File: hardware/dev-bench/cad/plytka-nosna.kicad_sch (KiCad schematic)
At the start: 69 parts, among them J1 ARDUINO POWER, J10 CC1120EM P2, J11 ANALIZATOR, J12 VTEST 0-15V, J2 ARDUINO A0-A5, J3 ARDUINO D0-D7, J4 ARDUINO D8-SCL, J5 DEVKITC J1, J6 DEVKITC J3, J7 SHARP LS027B7DH01A, J9 CC1120EM P1, Q1 MMBT3904, SW1 GÓRA, SW2 DÓŁ, SW3 OK, SW4 WSTECZ, SW5 CISZA, SW6 PRZYGOTOWANIE, U1 CY15B104QN-50SXI, U2 MCP1640

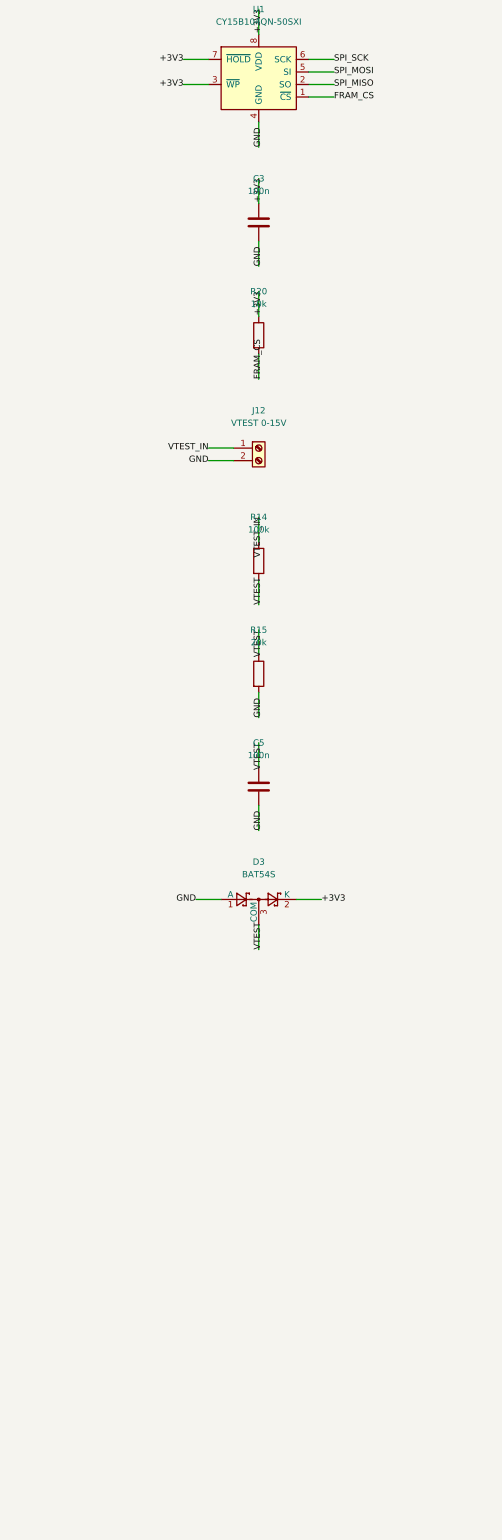
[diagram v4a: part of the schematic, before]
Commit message: Dev bench N1: hardware FRAM CS release on supply loss (audit vs F106)
The spec (elektronika.md, power loss, point 2) requires the FRAM CS to be
released before the FRAM supply drops below its minimum. The Arduino
RESET pin of the nRF52840-DK is not connected to the MCU (R45 not
fitted), so a supervisor on the MCU reset cannot do it on bench A.

- U3 TPS3840PH27 (push-pull active-high, 2.66-2.74 V) and U4 74LVC1G32
  force CS of U1 high below the threshold, independent of the MCU;
  C11/C12 decoupling; own TPS3840PH symbol (library WICI)
- bring-up steps F1-F3 (margin at 3.0 V, MR test, scope at power-off)
- docs: panel 5 V row in the supply table, 0.18 mm minimum track for
  the fabricator, SMD count, availability, reproduction record

Co-Authored-By: Claude Opus 5.5 <noreply@anthropic.com>
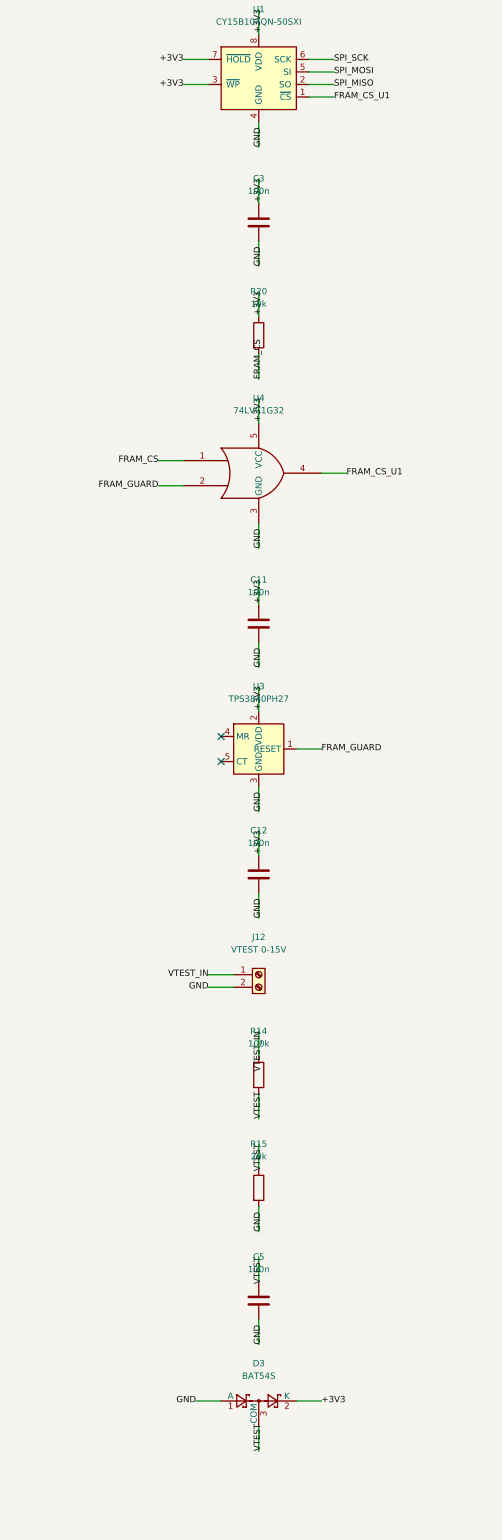
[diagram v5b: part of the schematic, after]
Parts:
- added C11, C12: 100n, Capacitor_SMD:C_0805_2012Metric, symbol Device:C
- added U3: TPS3840PH27, Package_TO_SOT_SMD:SOT-23-5, symbol WICI:TPS3840PH
- added U4: 74LVC1G32, Package_TO_SOT_SMD:SOT-23-5, symbol 74xGxx:74LVC1G32
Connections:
- net +3V3: now also C11.1, C12.1, U3.2 (VDD), U4.5 (VCC)
- net FRAM_CS: now also U4.1; no longer U1.1 (~{CS})
- net GND: now also C11.2, C12.2, U3.3 (GND), U4.3 (GND)
- new net FRAM_CS_U1: U1.1 (~{CS}), U4.4
- new net FRAM_GUARD: U3.1 (RESET), U4.2
- no-connect marks 48 -> 50
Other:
- moved on the sheet: C5, D3, J12, R14, R15

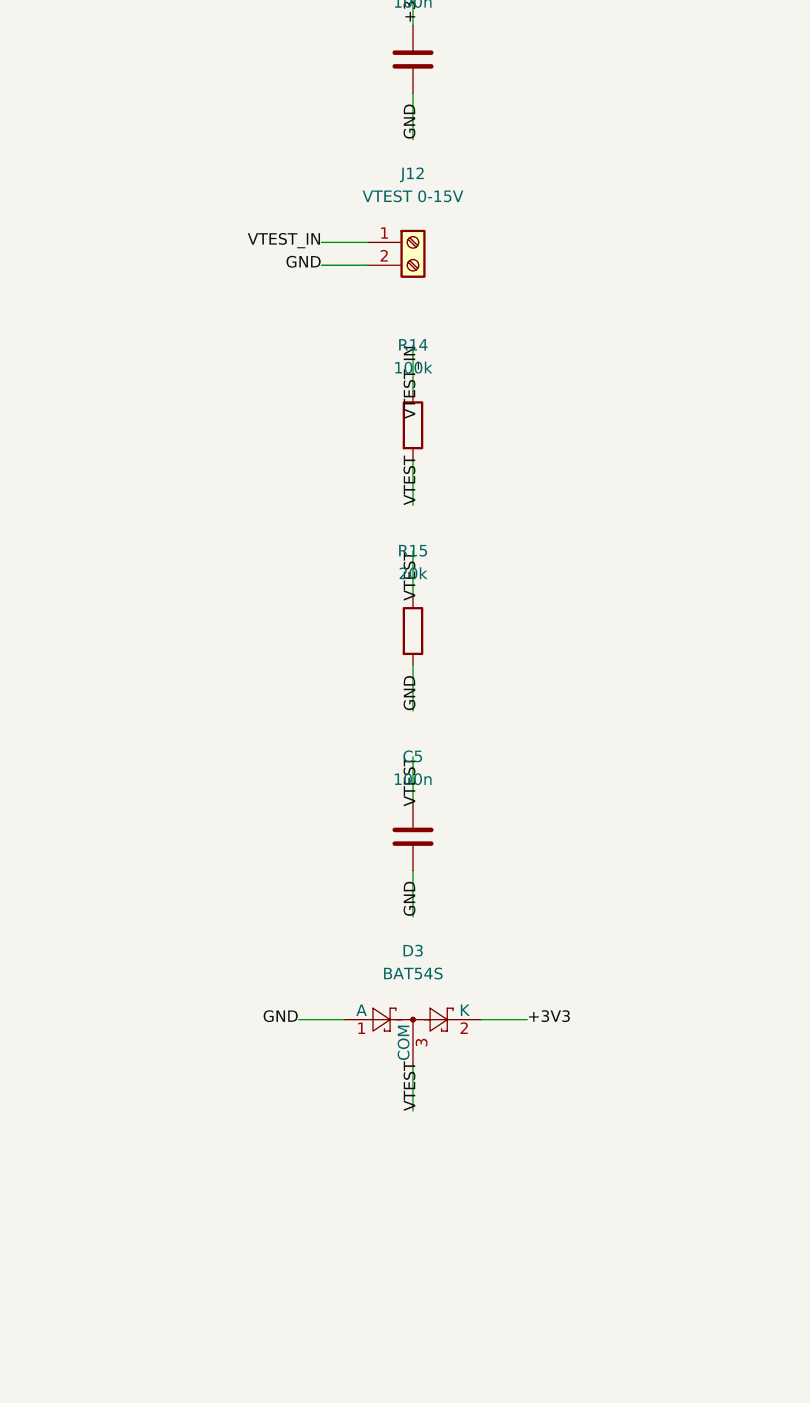
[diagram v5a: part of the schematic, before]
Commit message: Dev bench N1: hold-up capacitor for the FRAM guard response time
TPS3840 asserts up to 30 us after +3V3 is 10 % below its threshold
(2.394 V worst case, SNVSB03E table 6.6). With only the 0805 parts on
N1, +3V3 at 150 mA would reach the 2.0 V FRAM minimum in about 16 us.
C13 100 uF 10 V X5R 1210 (>= 32 uF after DC bias and tolerance) keeps
the 2.394-2.0 V fall at >= 100 us, 3.4x the supervisor delay.

F3 now checks the fall rate (<= 6.6 mV/us), CS high within 30 us of
2.394 V with +3V3 still >= 2.2 V, under the largest +3V3 load.

Co-Authored-By: Claude Opus 5.5 <noreply@anthropic.com>
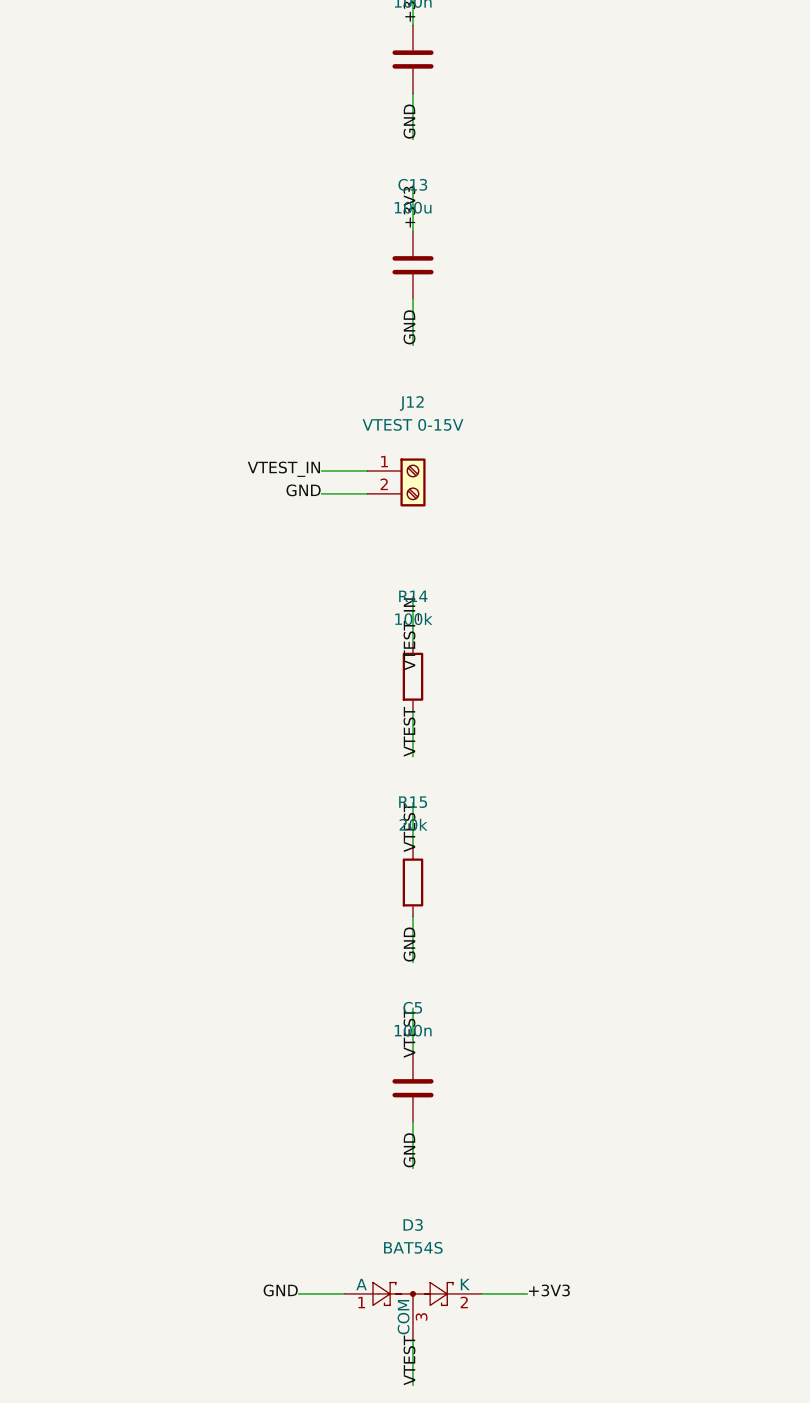
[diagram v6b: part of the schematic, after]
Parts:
- added C13: 100u, Capacitor_SMD:C_1210_3225Metric, symbol Device:C
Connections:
- net +3V3: now also C13.1
- net GND: now also C13.2
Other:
- moved on the sheet: C5, D3, J12, R14, R15
